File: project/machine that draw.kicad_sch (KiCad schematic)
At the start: 25 parts, among them J1 Moteur1, J10 Switch2, J11 Barrel_Jack_Switch, J12 Bouton Urgence, J2 FdC1, J3 SD_Card_Device, J4 Conn_01x02, J5 Conn_01x02, J6 Switch1, J7 OLED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

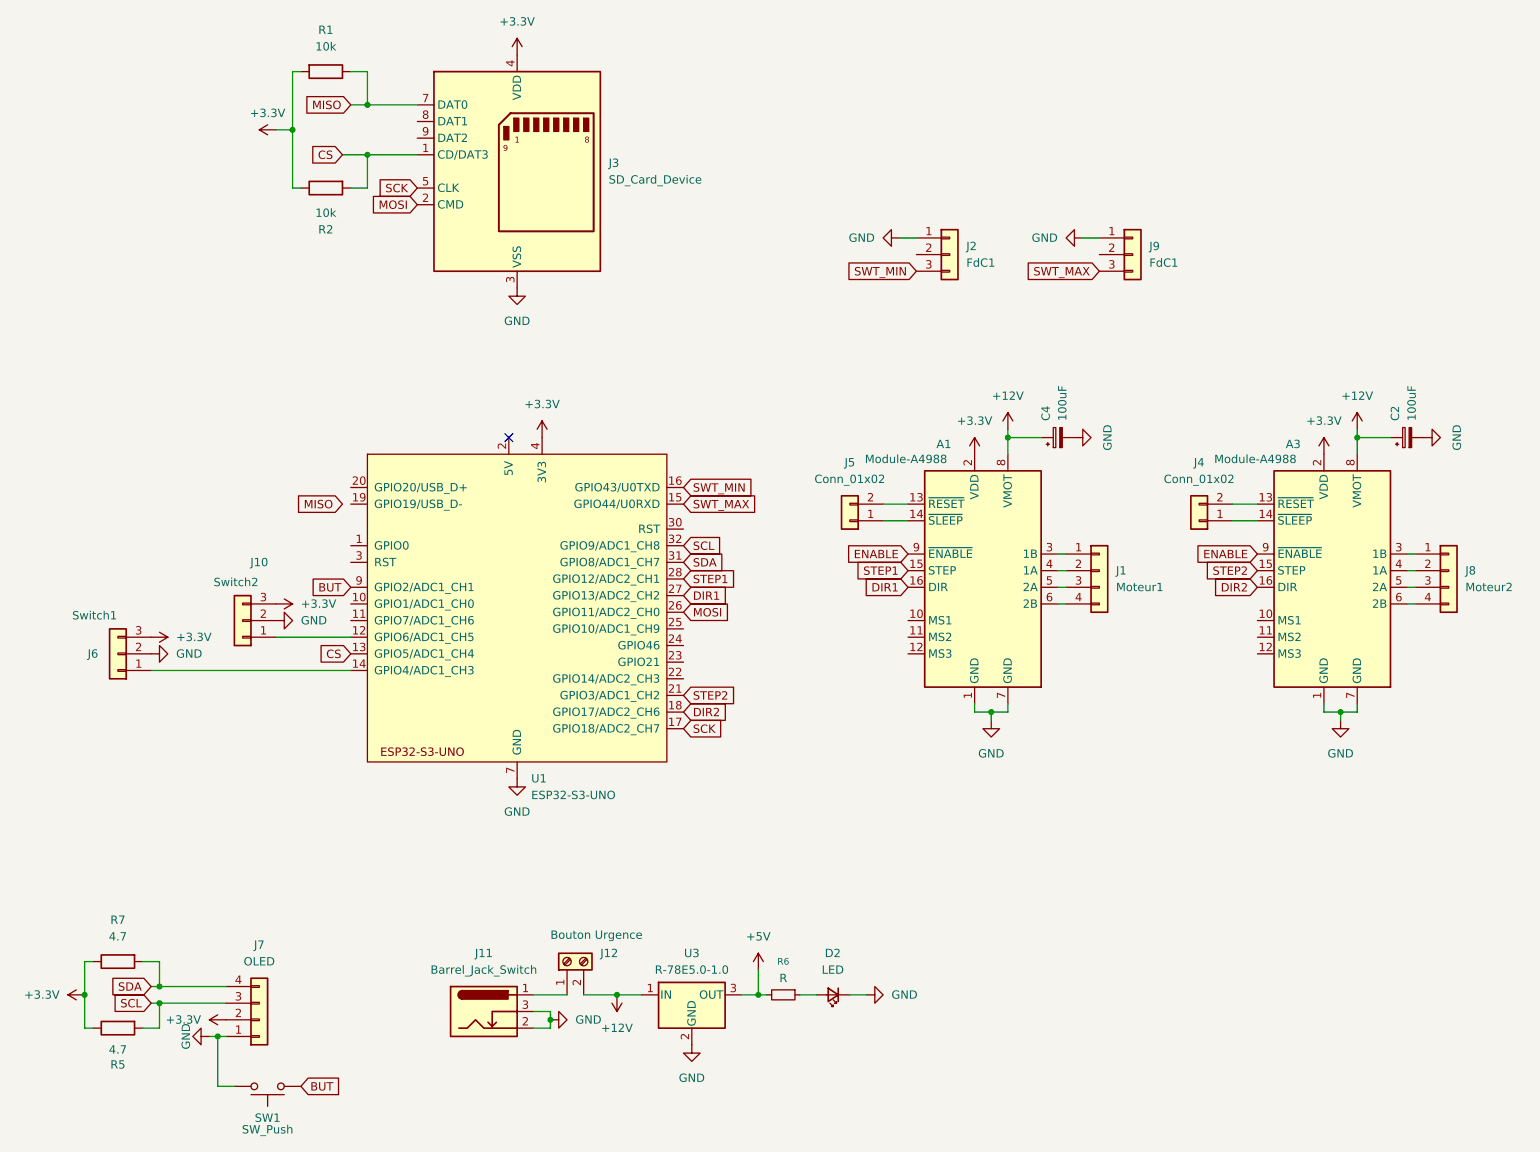
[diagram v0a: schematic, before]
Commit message: Correction schematic et création du fichier PCB
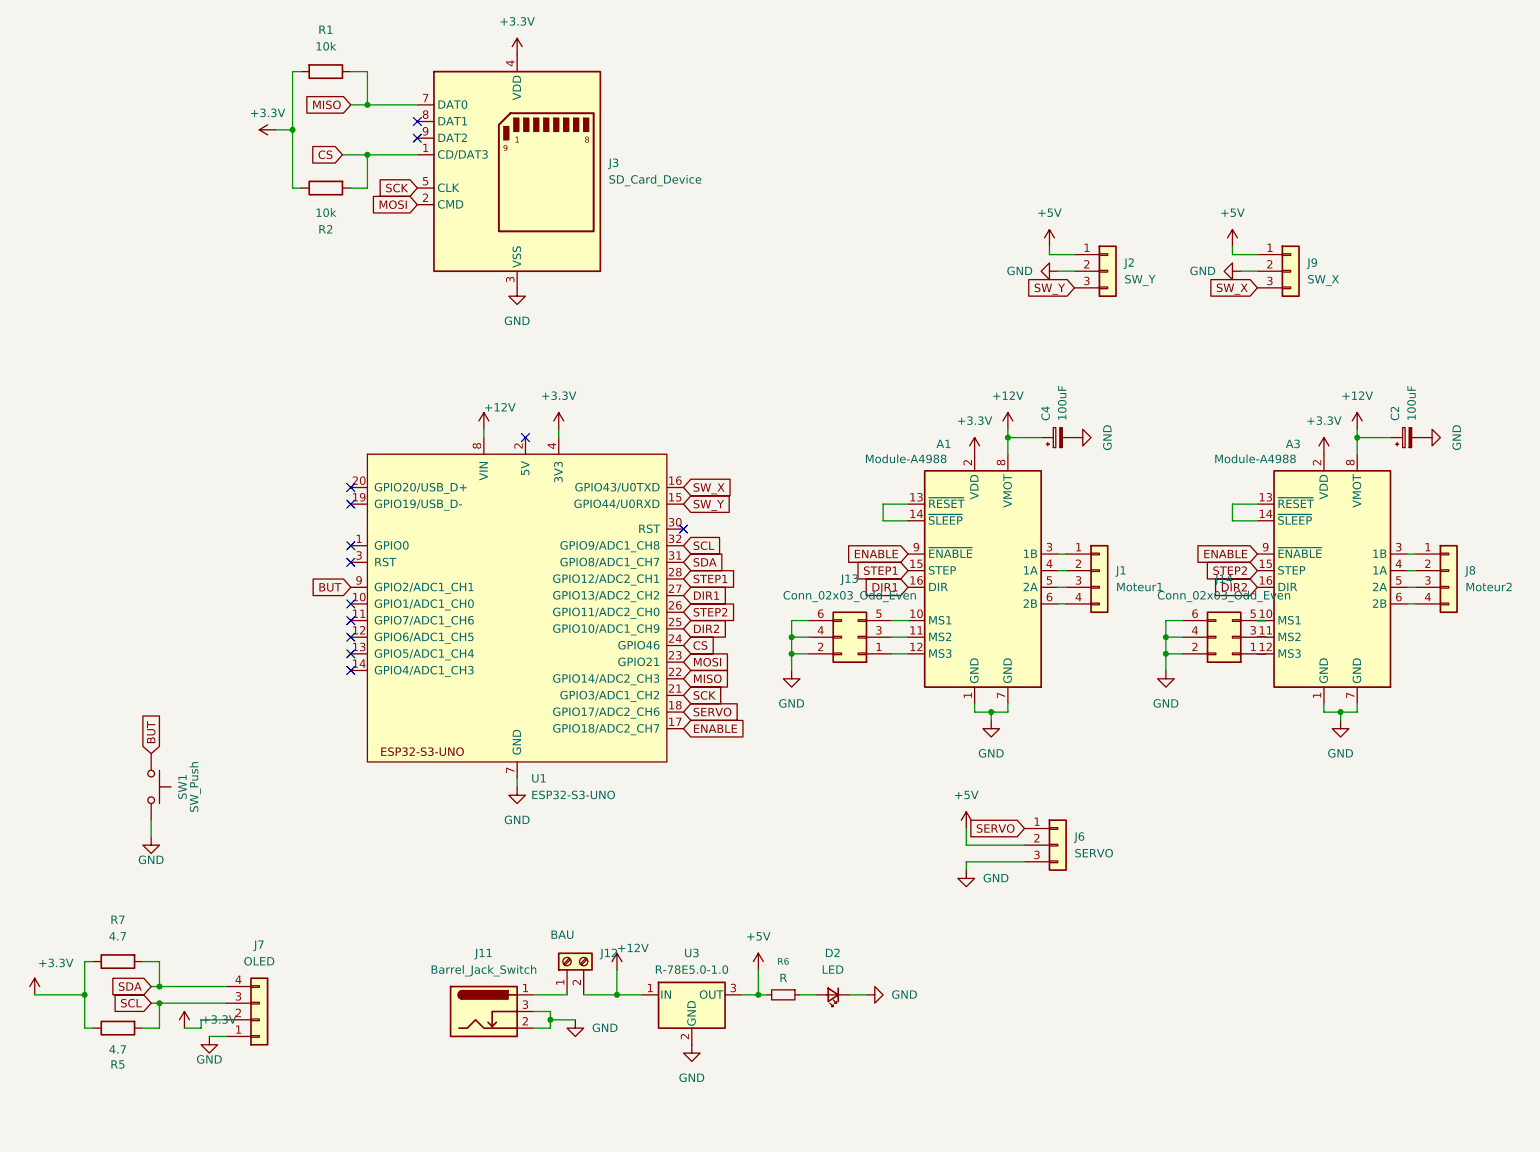
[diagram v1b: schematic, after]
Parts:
- removed J10: Switch2, Connector_PinSocket_2.54mm:PinSocket_1x03_P2.54mm_Vertical, symbol makerspace-unilasalle:Conn_01x03
- removed J4, J5: Conn_01x02, Connector_PinHeader_2.54mm:PinHeader_1x02_P2.54mm_Vertical, symbol makerspace-unilasalle:Conn_01x02
- added J13, J14: Conn_02x03_Odd_Even, Connector_PinHeader_2.54mm:PinHeader_2x03_P2.54mm_Vertical, symbol Connector_Generic:Conn_02x03_Odd_Even
- C2, C4: footprint (none) -> Capacitor_THT:CP_Radial_D8.0mm_P3.50mm
- D2: footprint (none) -> LED_SMD:LED_1206_3216Metric_Pad1.42x1.75mm_HandSolder
- J11: footprint (none) -> Connector_BarrelJack:BarrelJack_Horizontal
- J12: value Bouton Urgence -> BAU; footprint (none) -> TerminalBlock_Phoenix:TerminalBlock_Phoenix_PT-1,5-2-5.0-H_1x02_P5.00mm_Horizontal
- J2: value FdC1 -> SW_Y; footprint (none) -> Connector_PinHeader_2.54mm:PinHeader_1x03_P2.54mm_Vertical
- J3: footprint (none) -> makerspace-unilasalle:SD_Hirose_DM1AA_SF_PEJ82
- J6: value Switch1 -> SERVO; footprint Connector_PinSocket_2.54mm:PinSocket_1x03_P2.54mm_Vertical -> Connector_PinHeader_2.54mm:PinHeader_1x03_P2.54mm_Vertical
- J9: value FdC1 -> SW_X; footprint (none) -> Connector_PinHeader_2.54mm:PinHeader_1x03_P2.54mm_Vertical
- R1, R2, R5, R6, R7: footprint (none) -> makerspace-unilasalle:R_1206
- SW1: footprint (none) -> makerspace-unilasalle:SW_Push_KMR2
- U1: footprint PCM_Espressif:ESP32-S3-DevKitC -> makerspace-unilasalle:ESP_S3_UNO
- U3: footprint Converter_DCDC:Converter_DCDC_RECOM_R-78E-0.5_THT -> makerspace-unilasalle:Converter_DCDC_RECOM_R-78E-0.5_THT
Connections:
- net +12V: now also U1.8 (VIN)
- net +3.3V: no longer J6.3 (Pin_3)
- net +5V: now also J2.1 (Pin_1), J6.2 (Pin_2), J9.1 (Pin_1)
- net CS: now also U1.24 (GPIO46); no longer U1.13 (GPIO5/ADC1_CH4)
- net DIR2: now also U1.25 (GPIO10/ADC1_CH9); no longer U1.18 (GPIO17/ADC2_CH6)
- net ENABLE: now also U1.17 (GPIO18/ADC2_CH7)
- net GND: now also J2.2 (Pin_2), J6.3 (Pin_3), J9.2 (Pin_2), J13.2 (Pin_2), J13.4 (Pin_4), J13.6 (Pin_6), J14.2 (Pin_2), J14.4 (Pin_4), J14.6 (Pin_6); no longer J2.1 (Pin_1), J6.2 (Pin_2), J9.1 (Pin_1)
- net MISO: now also U1.22 (GPIO14/ADC2_CH3)
- net MOSI: now also U1.23 (GPIO21); no longer U1.26 (GPIO11/ADC2_CH0)
- net SCK: now also U1.21 (GPIO3/ADC1_CH2); no longer U1.17 (GPIO18/ADC2_CH7)
- net STEP2: now also U1.26 (GPIO11/ADC2_CH0); no longer U1.21 (GPIO3/ADC1_CH2)
- net at A1.14 (~{SLEEP}): now also A1.13 (~{RESET})
- net at A3.14 (~{SLEEP}): now also A3.13 (~{RESET})
- net at U1.14 (GPIO4/ADC1_CH3): no longer J6.1 (Pin_1)
- net at A3.10 (MS1): now also J14.5 (Pin_5)
- net at A3.11 (MS2): now also J14.3 (Pin_3)
- net at A3.12 (MS3): now also J14.1 (Pin_1)
- net at A1.10 (MS1): now also J13.5 (Pin_5)
- net at A1.11 (MS2): now also J13.3 (Pin_3)
- net at A1.12 (MS3): now also J13.1 (Pin_1)
- net SWT_MAX renamed SW_X
- net SW_X: now also U1.16 (GPIO43/U0TXD); no longer U1.15 (GPIO44/U0RXD)
- net SWT_MIN renamed SW_Y
- net SW_Y: now also U1.15 (GPIO44/U0RXD); no longer U1.16 (GPIO43/U0TXD)
- new net SERVO: J6.1 (Pin_1), U1.18 (GPIO17/ADC2_CH6)
- no-connect marks 1 -> 13
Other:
- moved on the sheet: J2, J9, SW1

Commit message: finalisation du pcb
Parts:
- removed SW1: SW_Push, makerspace-unilasalle:SW_Push_KMR2, symbol makerspace-unilasalle:SW_Push
- added C1, C3: 10uF, Capacitor_SMD:C_1206_3216Metric_Pad1.33x1.80mm_HandSolder, symbol Device:C_Small
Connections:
- net +12V: now also C1.1
- net +3.3V: now also J2.1 (Pin_1), J9.1 (Pin_1)
- net +5V: now also C3.1; no longer J2.1 (Pin_1), J9.1 (Pin_1)
- net DIR1: now also U1.28 (GPIO12/ADC2_CH1); no longer U1.27 (GPIO13/ADC2_CH2)
- net DIR2: now also U1.26 (GPIO11/ADC2_CH0); no longer U1.25 (GPIO10/ADC1_CH9)
- net GND: now also C1.2, C3.2
- net STEP1: now also U1.27 (GPIO13/ADC2_CH2); no longer U1.28 (GPIO12/ADC2_CH1)
- net STEP2: now also U1.25 (GPIO10/ADC1_CH9); no longer U1.26 (GPIO11/ADC2_CH0)
